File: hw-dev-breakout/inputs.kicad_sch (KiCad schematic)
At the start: 30 parts, among them J3 WAGO 250-216, U5 40106, U6 4049

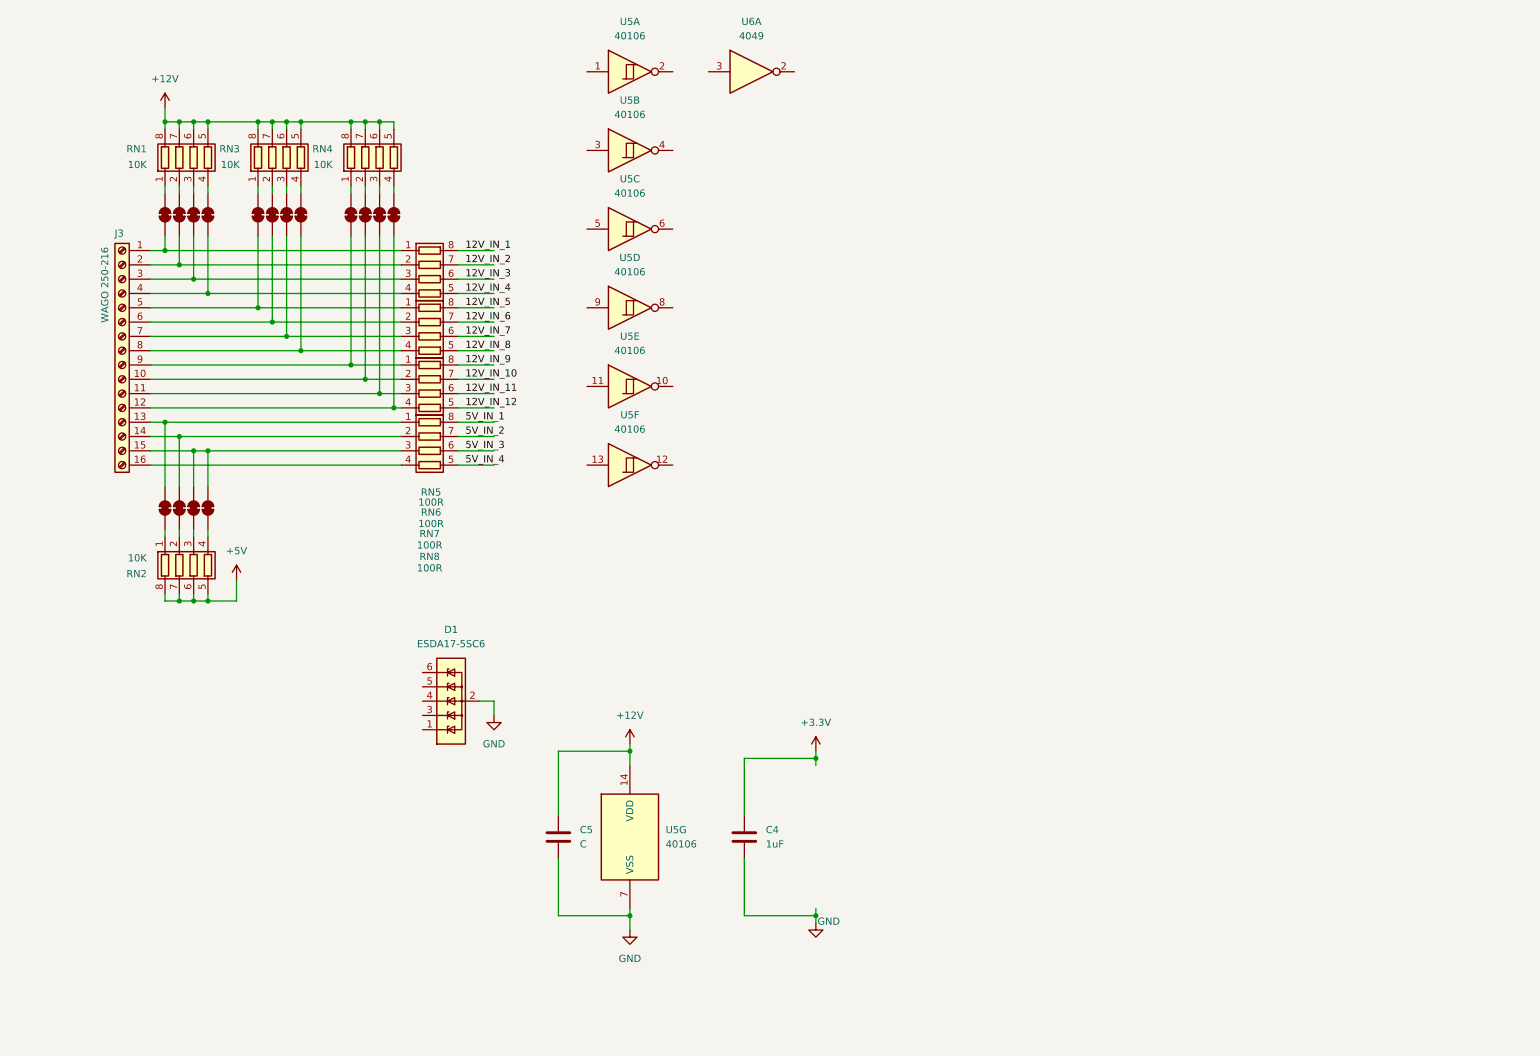
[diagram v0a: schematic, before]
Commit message: Schematic mostly done, pre-resistor pack swap
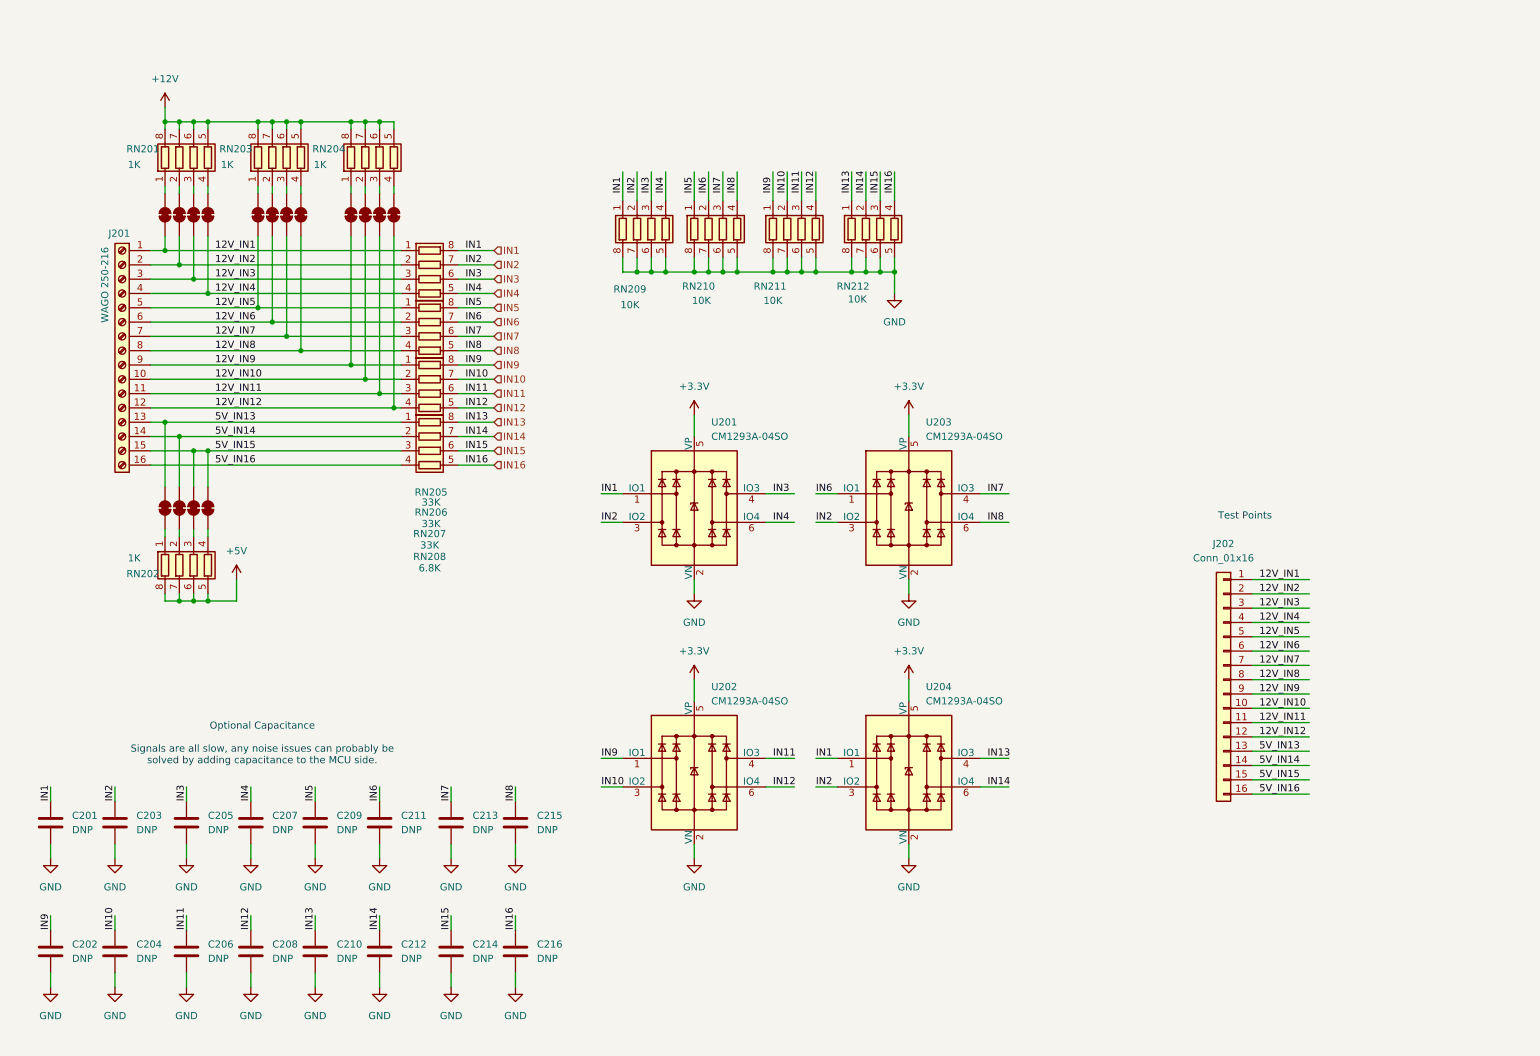
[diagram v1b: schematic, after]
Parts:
- removed C4: 1uF, symbol Device:C
- removed C5: C, symbol Device:C
- removed D1: ESDA17-5SC6, Package_TO_SOT_SMD:SOT-23-6, symbol Power_Protection:ESDA6V1-5SC6
- removed U5: 40106, symbol 4xxx:40106
- removed U6: 4049, symbol 4xxx:4049
- added C201, C202, C203, C204, C205, C206, C207, C208, C209, C210, C211, C212, C213, C214, C215, C216: DNP, Capacitor_SMD:C_0603_1608Metric, symbol Device:C
- added J202: Conn_01x16, Connector_PinHeader_2.54mm:PinHeader_1x01_P2.54mm_Vertical, symbol Connector_Generic:Conn_01x16
- added RN209, RN210, RN211, RN212: 10K, Resistor_SMD:R_Array_Convex_4x0603, symbol Device:R_Pack04
- added U201, U202, U203, U204: CM1293A-04SO, Package_TO_SOT_SMD:SOT-23-6, symbol Power_Protection:CDSOT236-0504C
- JP201: renamed from JP1; footprint (none) -> Jumper:SolderJumper-2_P1.3mm_Bridged_Pad1.0x1.5mm
- JP202: renamed from JP2; footprint (none) -> Jumper:SolderJumper-2_P1.3mm_Bridged_Pad1.0x1.5mm
- JP203: renamed from JP3; footprint (none) -> Jumper:SolderJumper-2_P1.3mm_Bridged_Pad1.0x1.5mm
- JP204: renamed from JP4; footprint (none) -> Jumper:SolderJumper-2_P1.3mm_Bridged_Pad1.0x1.5mm
- JP205: renamed from JP5; footprint (none) -> Jumper:SolderJumper-2_P1.3mm_Bridged_Pad1.0x1.5mm
- JP206: renamed from JP6; footprint (none) -> Jumper:SolderJumper-2_P1.3mm_Bridged_Pad1.0x1.5mm
- JP207: renamed from JP7; footprint (none) -> Jumper:SolderJumper-2_P1.3mm_Bridged_Pad1.0x1.5mm
- JP208: renamed from JP8; footprint (none) -> Jumper:SolderJumper-2_P1.3mm_Bridged_Pad1.0x1.5mm
- JP209: renamed from JP9; footprint (none) -> Jumper:SolderJumper-2_P1.3mm_Bridged_Pad1.0x1.5mm
- JP210: renamed from JP10; footprint (none) -> Jumper:SolderJumper-2_P1.3mm_Bridged_Pad1.0x1.5mm
- JP211: renamed from JP11; footprint (none) -> Jumper:SolderJumper-2_P1.3mm_Bridged_Pad1.0x1.5mm
- JP212: renamed from JP12; footprint (none) -> Jumper:SolderJumper-2_P1.3mm_Bridged_Pad1.0x1.5mm
- JP213: renamed from JP13; footprint (none) -> Jumper:SolderJumper-2_P1.3mm_Bridged_Pad1.0x1.5mm
- JP214: renamed from JP14; footprint (none) -> Jumper:SolderJumper-2_P1.3mm_Bridged_Pad1.0x1.5mm
- JP215: renamed from JP15; footprint (none) -> Jumper:SolderJumper-2_P1.3mm_Bridged_Pad1.0x1.5mm
- JP216: renamed from JP16; footprint (none) -> Jumper:SolderJumper-2_P1.3mm_Bridged_Pad1.0x1.5mm
- RN201: renamed from RN1; value 10K -> 1K; footprint (none) -> Resistor_SMD:R_Array_Convex_4x0603
- RN202: renamed from RN2; value 10K -> 1K; footprint (none) -> Resistor_SMD:R_Array_Convex_4x0603
- RN203: renamed from RN3; value 10K -> 1K; footprint (none) -> Resistor_SMD:R_Array_Convex_4x0603
- RN204: renamed from RN4; value 10K -> 1K; footprint (none) -> Resistor_SMD:R_Array_Convex_4x0603
- RN205: renamed from RN5; value 100R -> 33K; footprint (none) -> Resistor_SMD:R_Array_Convex_4x0603
- RN206: renamed from RN6; value 100R -> 33K; footprint (none) -> Resistor_SMD:R_Array_Convex_4x0603
- RN207: renamed from RN7; value 100R -> 33K; footprint (none) -> Resistor_SMD:R_Array_Convex_4x0603
- RN208: renamed from RN8; value 100R -> 6.8K; footprint (none) -> Resistor_SMD:R_Array_Convex_4x0603
- renumbered J3 to J201
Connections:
- net +3.3V: now also U201.5 (VP), U202.5 (VP), U203.5 (VP), U204.5 (VP)
- net GND: now also C201.2, C202.2, C203.2, C204.2, C205.2, C206.2, C207.2, C208.2, C209.2, C210.2, C211.2, C212.2, C213.2, C214.2, C215.2, C216.2, RN209.5 (R4.2), RN209.6 (R3.2), RN209.7 (R2.2), RN209.8 (R1.2), RN210.5 (R4.2), RN210.6 (R3.2), RN210.7 (R2.2), RN210.8 (R1.2), RN211.5 (R4.2), RN211.6 (R3.2), RN211.7 (R2.2), RN211.8 (R1.2), RN212.5 (R4.2), RN212.6 (R3.2), RN212.7 (R2.2), RN212.8 (R1.2), U201.2 (VN), U202.2 (VN), U203.2 (VN), U204.2 (VN)
- net 12V_IN6: now reaches J201.6 (Pin_6), JP210.1 (A), RN206.2 (R2.1)
- net 12V_IN6: now also J202.6 (Pin_6)
- net 12V_IN10: now reaches J201.10 (Pin_10), JP214.1 (A), RN207.2 (R2.1)
- net 12V_IN10: now also J202.10 (Pin_10)
- net 5V_IN14: now reaches J201.14 (Pin_14), JP204.2 (B), RN208.2 (R2.1)
- net 5V_IN14: now also J202.14 (Pin_14)
- net 5V_IN13: now reaches J201.13 (Pin_13), JP202.2 (B), RN208.1 (R1.1)
- net 5V_IN13: now also J202.13 (Pin_13)
- net 5V_IN15: now reaches J201.15 (Pin_15), JP206.2 (B), JP208.2 (B), RN208.3 (R3.1)
- net 5V_IN15: now also J202.15 (Pin_15)
- net 5V_IN16: now reaches J201.16 (Pin_16), RN208.4 (R4.1)
- net 5V_IN16: now also J202.16 (Pin_16)
- net 12V_IN4: now reaches J201.4 (Pin_4), JP207.1 (A), RN205.4 (R4.1)
- net 12V_IN4: now also J202.4 (Pin_4)
- net 12V_IN9: now reaches J201.9 (Pin_9), JP213.1 (A), RN207.1 (R1.1)
- net 12V_IN9: now also J202.9 (Pin_9)
- net 12V_IN11: now reaches J201.11 (Pin_11), JP215.1 (A), RN207.3 (R3.1)
- net 12V_IN11: now also J202.11 (Pin_11)
- net 12V_IN12: now reaches J201.12 (Pin_12), JP216.1 (A), RN207.4 (R4.1)
- net 12V_IN12: now also J202.12 (Pin_12)
- net 12V_IN3: now reaches J201.3 (Pin_3), JP205.1 (A), RN205.3 (R3.1)
- net 12V_IN3: now also J202.3 (Pin_3)
- net 12V_IN7: now reaches J201.7 (Pin_7), JP211.1 (A), RN206.3 (R3.1)
- net 12V_IN7: now also J202.7 (Pin_7)
- net 12V_IN1: now reaches J201.1 (Pin_1), JP201.1 (A), RN205.1 (R1.1)
- net 12V_IN1: now also J202.1 (Pin_1)
- net 12V_IN5: now reaches J201.5 (Pin_5), JP209.1 (A), RN206.1 (R1.1)
- net 12V_IN5: now also J202.5 (Pin_5)
- net 12V_IN8: now reaches J201.8 (Pin_8), JP212.1 (A), RN206.4 (R4.1)
- net 12V_IN8: now also J202.8 (Pin_8)
- net 12V_IN2: now reaches J201.2 (Pin_2), JP203.1 (A), RN205.2 (R2.1)
- net 12V_IN2: now also J202.2 (Pin_2)
- net 12V_IN_1 renamed IN1
- net IN1: now also C201.1, RN209.1 (R1.1), U201.1 (IO1), U204.1 (IO1)
- net 12V_IN_10 renamed IN10
- net IN10: now also C204.1, RN211.2 (R2.1), U202.3 (IO2)
- net 12V_IN_11 renamed IN11
- net IN11: now also C206.1, RN211.3 (R3.1), U202.4 (IO3)
- net 12V_IN_12 renamed IN12
- net IN12: now also C208.1, RN211.4 (R4.1), U202.6 (IO4)
- net 12V_IN_2 renamed IN2
- net IN2: now also C203.1, RN209.2 (R2.1), U201.3 (IO2), U203.3 (IO2), U204.3 (IO2)
- net 12V_IN_3 renamed IN3
- net IN3: now also C205.1, RN209.3 (R3.1), U201.4 (IO3)
- net 12V_IN_4 renamed IN4
- net IN4: now also C207.1, RN209.4 (R4.1), U201.6 (IO4)
- net 12V_IN_5 renamed IN5
- net IN5: now also C209.1, RN210.1 (R1.1)
- net 12V_IN_6 renamed IN6
- net IN6: now also C211.1, RN210.2 (R2.1), U203.1 (IO1)
- net 12V_IN_7 renamed IN7
- net IN7: now also C213.1, RN210.3 (R3.1), U203.4 (IO3)
- net 12V_IN_8 renamed IN8
- net IN8: now also C215.1, RN210.4 (R4.1), U203.6 (IO4)
- net 12V_IN_9 renamed IN9
- net IN9: now also C202.1, RN211.1 (R1.1), U202.1 (IO1)
- net 5V_IN_1 renamed IN13
- net IN13: now also C210.1, RN212.1 (R1.1), U204.4 (IO3)
- net 5V_IN_2 renamed IN14
- net IN14: now also C212.1, RN212.2 (R2.1), U204.6 (IO4)
- net 5V_IN_3 renamed IN15
- net IN15: now also C214.1, RN212.3 (R3.1)
- net 5V_IN_4 renamed IN16
- net IN16: now also C216.1, RN212.4 (R4.1)
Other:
- note added: "Optional Capacitance Signals are all slow, any noise issues can probably be solved by adding capacitance to the MCU side."
- note added: "Test Points"

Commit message: Complete schematic with footprint assignments
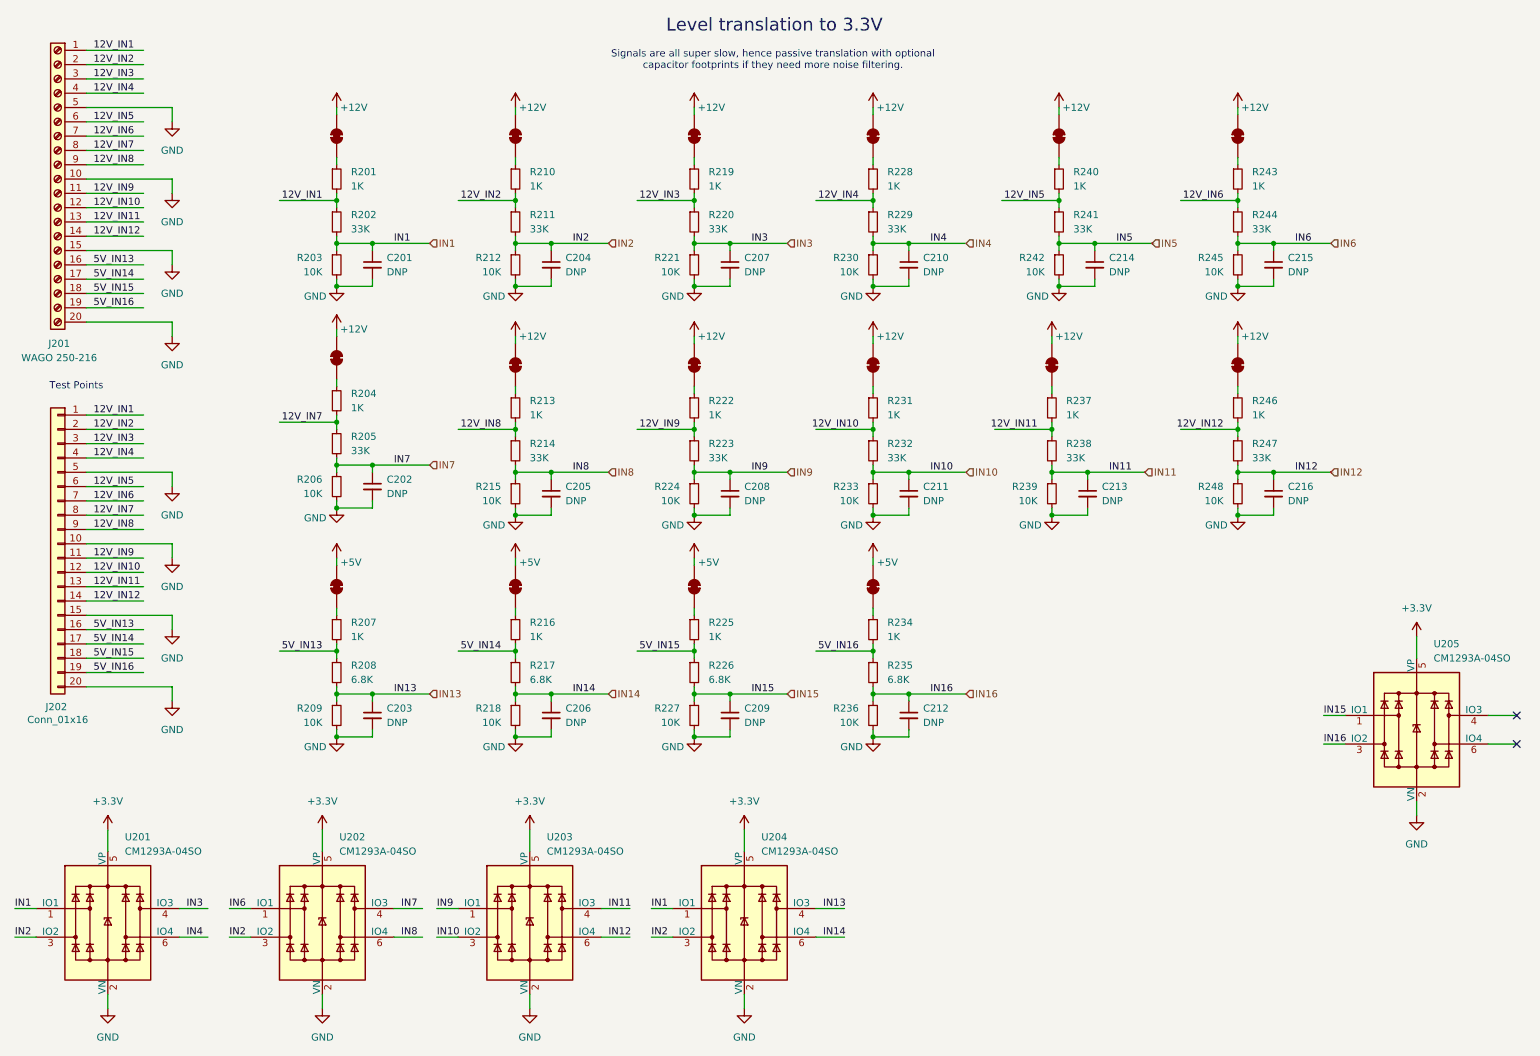
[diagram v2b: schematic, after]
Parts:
- removed C201, C202, C203, C204, C205, C206, C207, C208, C209, C210, C211, C212, C213, C214, C216: DNP, Capacitor_SMD:C_0603_1608Metric, symbol Device:C
- removed RN201, RN202, RN203, RN204: 1K, Resistor_SMD:R_Array_Convex_4x0603, symbol Device:R_Pack04
- removed RN205, RN206, RN207: 33K, Resistor_SMD:R_Array_Convex_4x0603, symbol Device:R_Pack04
- removed RN208: 6.8K, Resistor_SMD:R_Array_Convex_4x0603, symbol Device:R_Pack04
- removed RN209, RN210, RN211, RN212: 10K, Resistor_SMD:R_Array_Convex_4x0603, symbol Device:R_Pack04
- added C202, C203, C204, C205, C206, C207, C208, C209, C210, C211, C212, C213, C214, C215, C216: DNP, Capacitor_SMD:C_0603_1608Metric, symbol Device:C_Small
- added R201, R204, R207, R210, R213, R216, R219, R222, R225, R228, R231, R234, R237, R240, R243, R246: 1K, Resistor_SMD:R_0603_1608Metric, symbol Device:R_Small
- added R202, R205, R211, R214, R220, R223, R229, R232, R238, R241, R244, R247: 33K, Resistor_SMD:R_0603_1608Metric, symbol Device:R_Small
- added R203, R206, R209, R212, R215, R218, R221, R224, R227, R230, R233, R236, R239, R242, R245, R248: 10K, Resistor_SMD:R_0603_1608Metric, symbol Device:R_Small
- added R208, R217, R226, R235: 6.8K, Resistor_SMD:R_0603_1608Metric, symbol Device:R_Small
- added U205: CM1293A-04SO, Package_TO_SOT_SMD:SOT-23-6, symbol Power_Protection:CDSOT236-0504C
- C201: renamed from C215; symbol Device:C -> Device:C_Small
- J201: footprint (none) -> hw-dev-breakout:CONN-TH_250-220; symbol Connector:Screw_Terminal_01x16 -> Connector:Screw_Terminal_01x20
- J202: symbol Connector_Generic:Conn_01x16 -> Connector_Generic:Conn_01x20
- renumbered U203 to U202, U202 to U203
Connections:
- net +12V: now also JP201.2 (B), JP202.2 (B), JP204.2 (B), JP205.2 (B), JP207.2 (B), JP208.2 (B), JP210.2 (B), JP211.2 (B), JP213.2 (B), JP214.2 (B), JP215.2 (B), JP216.2 (B)
- net +3.3V: now also U205.5 (VP)
- net +5V: now also JP203.2 (B), JP206.2 (B), JP209.2 (B), JP212.2 (B)
- net 12V_IN1: now also R201.2, R202.1; no longer JP201.1 (A)
- net 12V_IN10: now also J201.12 (Pin_12), J202.12 (Pin_12), R231.2, R232.1; no longer J201.10 (Pin_10), J202.10 (Pin_10), JP214.1 (A)
- net 12V_IN11: now also J201.13 (Pin_13), J202.13 (Pin_13), R237.2, R238.1; no longer J201.11 (Pin_11), J202.11 (Pin_11), JP215.1 (A)
- net 12V_IN12: now also J201.14 (Pin_14), J202.14 (Pin_14), R246.2, R247.1; no longer J201.12 (Pin_12), J202.12 (Pin_12), JP216.1 (A)
- net 12V_IN2: now also R210.2, R211.1; no longer JP203.1 (A)
- net 12V_IN3: now also R219.2, R220.1; no longer JP205.1 (A)
- net 12V_IN4: now also R228.2, R229.1; no longer JP207.1 (A)
- net 12V_IN5: now also J201.6 (Pin_6), J202.6 (Pin_6), R240.2, R241.1; no longer J201.5 (Pin_5), J202.5 (Pin_5), JP209.1 (A)
- net 12V_IN6: now also J201.7 (Pin_7), J202.7 (Pin_7), R243.2, R244.1; no longer J201.6 (Pin_6), J202.6 (Pin_6), JP210.1 (A)
- net 12V_IN7: now also J201.8 (Pin_8), J202.8 (Pin_8), R204.2, R205.1; no longer J201.7 (Pin_7), J202.7 (Pin_7), JP211.1 (A)
- net 12V_IN8: now also J201.9 (Pin_9), J202.9 (Pin_9), R213.2, R214.1; no longer J201.8 (Pin_8), J202.8 (Pin_8), JP212.1 (A)
- net 12V_IN9: now also J201.11 (Pin_11), J202.11 (Pin_11), R222.2, R223.1; no longer J201.9 (Pin_9), J202.9 (Pin_9), JP213.1 (A)
- net 5V_IN13: now also J201.16 (Pin_16), J202.16 (Pin_16), R207.2, R208.1; no longer J201.13 (Pin_13), J202.13 (Pin_13), JP202.2 (B)
- net 5V_IN14: now also J201.17 (Pin_17), J202.17 (Pin_17), R216.2, R217.1; no longer J201.14 (Pin_14), J202.14 (Pin_14), JP204.2 (B)
- net 5V_IN15: now also J201.18 (Pin_18), J202.18 (Pin_18), R225.2, R226.1; no longer J201.15 (Pin_15), J202.15 (Pin_15), JP206.2 (B), JP208.2 (B)
- net 5V_IN16: now also J201.19 (Pin_19), J202.19 (Pin_19), R234.2, R235.1; no longer J201.16 (Pin_16), J202.16 (Pin_16)
- net GND: now also J201.10 (Pin_10), J201.15 (Pin_15), J201.20 (Pin_20), J201.5 (Pin_5), J202.10 (Pin_10), J202.15 (Pin_15), J202.20 (Pin_20), J202.5 (Pin_5), C202.2, C203.2, C204.2, C205.2, C206.2, C207.2, C208.2, C209.2, C210.2, C211.2, C212.2, C213.2, C214.2, C215.2, C216.2, R203.2, R206.2, R209.2, R212.2, R215.2, R218.2, R221.2, R224.2, R227.2, R230.2, R233.2, R236.2, R239.2, R242.2, R245.2, R248.2, U205.2 (VN)
- net IN1: now also C201.1, R202.2, R203.1
- net IN10: now also C211.1, R232.2, R233.1
- net IN11: now also C213.1, R238.2, R239.1
- net IN12: now also C214.1, C216.1, R241.2, R242.1, R247.2, R248.1
- net IN13: now also C203.1, R208.2, R209.1
- net IN14: now also C206.1, R217.2, R218.1
- net IN15: now also C209.1, R226.2, R227.1, U205.1 (IO1)
- net IN16: now also C212.1, R235.2, R236.1, U205.3 (IO2)
- net IN2: now also C204.1, R211.2, R212.1
- net IN3: now also C207.1, R220.2, R221.1
- net IN4: now also C210.1, R229.2, R230.1
- net IN6: now also C215.1, R244.2, R245.1
- net IN7: now also C202.1, R205.2, R206.1
- net IN8: now also C205.1, R214.2, R215.1; no longer C201.1
- net IN9: now also C208.1, R223.2, R224.1
- net at JP204.1 (A): now also R210.1
- net at JP206.1 (A): now also R216.1
- net at JP208.1 (A): now also R222.1
- net at JP202.1 (A): now also R204.1
- new net: JP205.1 (A), R213.1
- new net: JP203.1 (A), R207.1
- new net: JP209.1 (A), R225.1
- new net: JP207.1 (A), R219.1
- new net: JP212.1 (A), R234.1
- new net: JP216.1 (A), R246.1
- new net: JP210.1 (A), R228.1
- new net: JP211.1 (A), R231.1
- new net: JP213.1 (A), R237.1
- new net: JP215.1 (A), R243.1
- new net: JP201.1 (A), R201.1
- new net: JP214.1 (A), R240.1
- no-connect marks 0 -> 2
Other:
- note added: "Level translation to 3.3V"
- note added: "Signals are all super slow, hence passive translation with optional capacitor footprints if they need more noise filtering."
- note removed: "Optional Capacitance Signals are all slow, any noise issues can probably be solved by adding capacitance to the MCU side."
- moved on the sheet: C201, U201, U202, U203, U204
